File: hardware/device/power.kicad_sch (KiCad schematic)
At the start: 46 parts, among them IC3 SP3401-02UTG, J1 POT_CONN, J2 USB, U20 TPS62A02DRL, U21 TPS560200, U22 BQ24072RGT, U23 BQ21040DBV, U26 BQ25040, U31 FUSB302B01MPX, U32 LTC2942

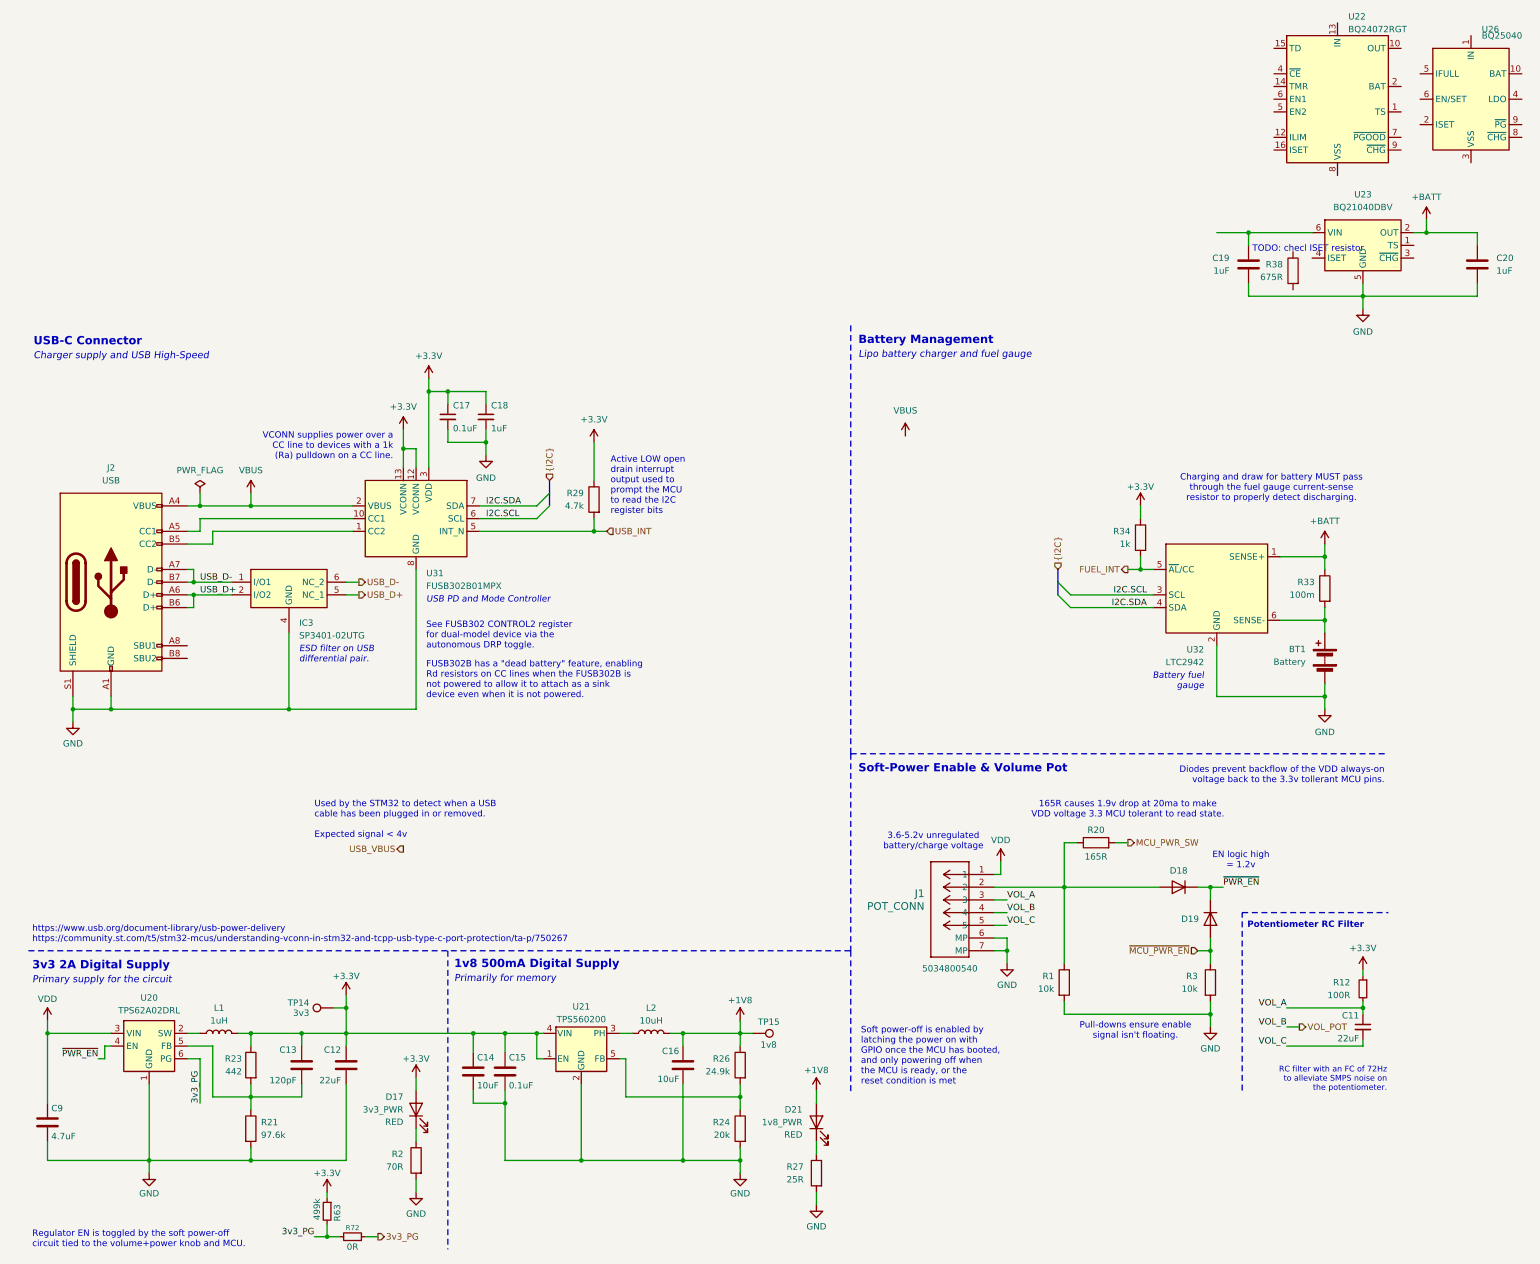
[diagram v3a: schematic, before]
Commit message: feat: various routing, footprint and schematic cleanup
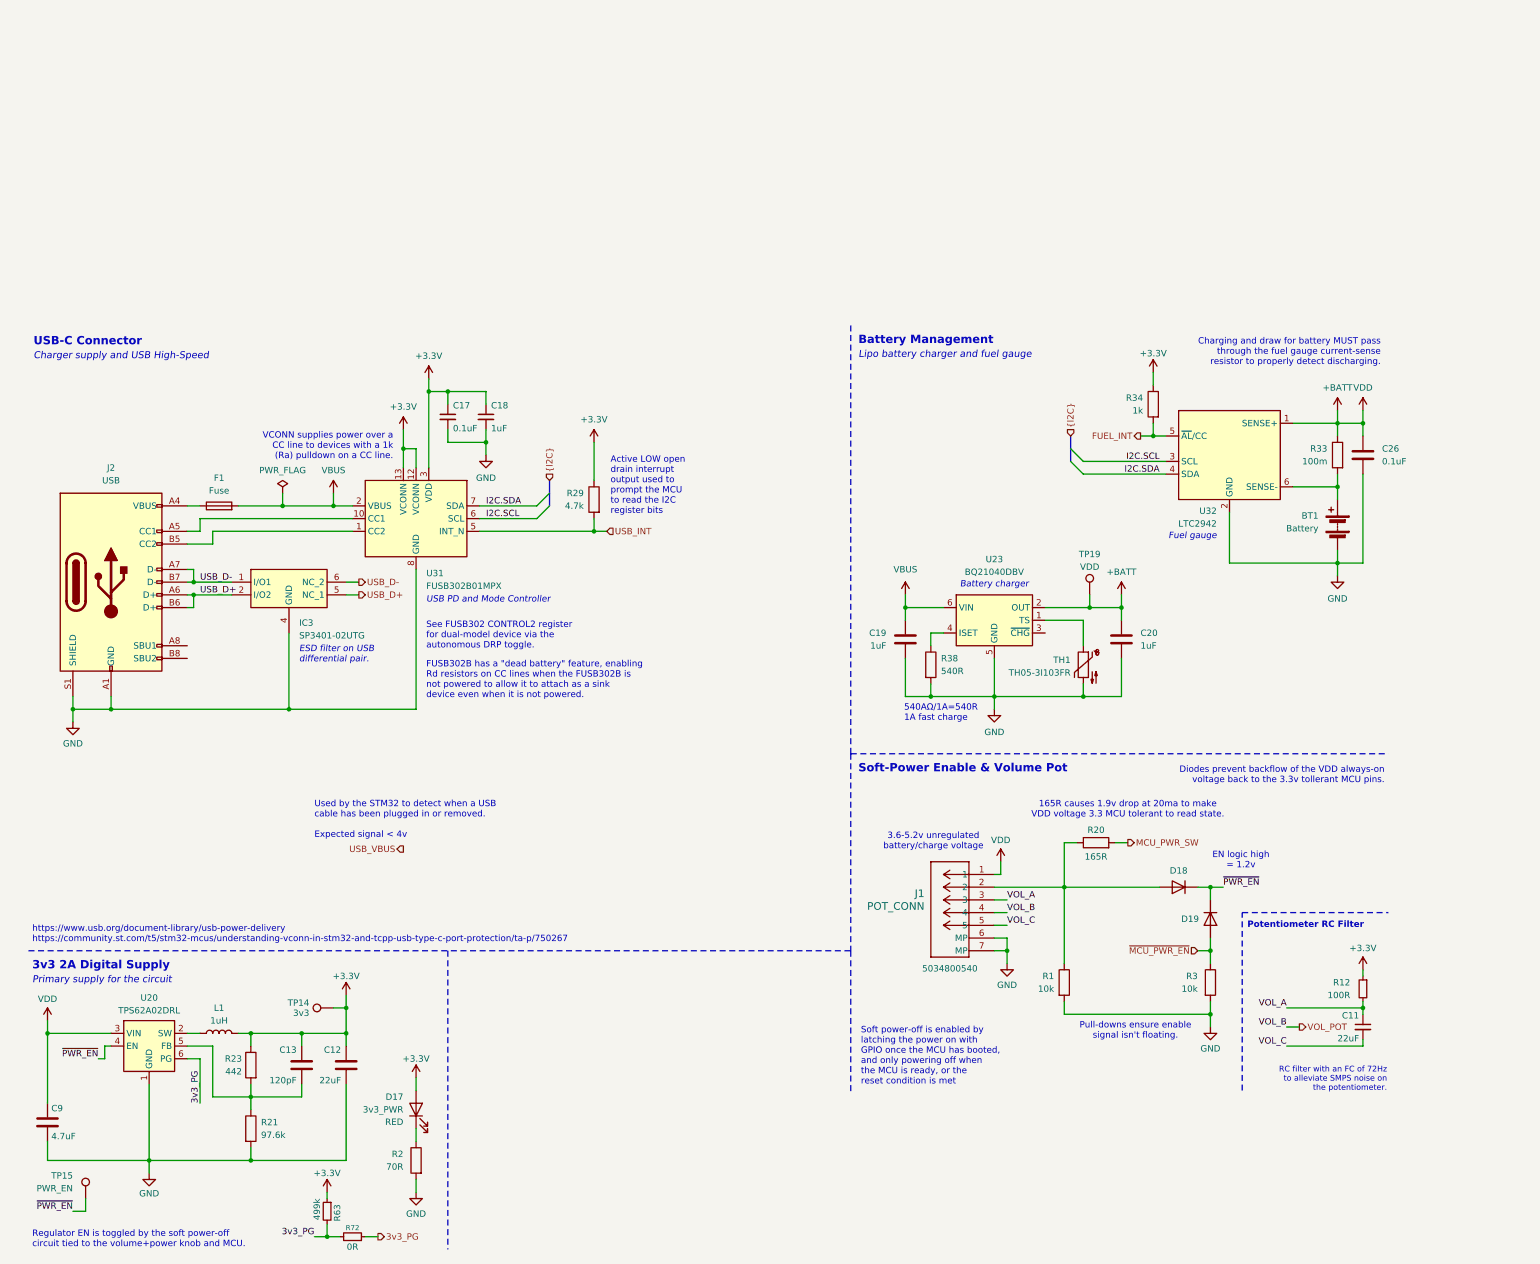
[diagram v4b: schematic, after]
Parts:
- removed C14, C16: 10uF, Capacitor_SMD:C_0402_1005Metric, symbol Device:C
- removed C15: 0.1uF, Capacitor_SMD:C_0402_1005Metric, symbol Device:C
- removed D21: 1v8_PWR, LED_SMD:LED_0805_2012Metric_Pad1.15x1.40mm_HandSolder, symbol Device:LED
- removed L2: 10uH, symbol Device:L
- removed R24: 20k, Capacitor_SMD:C_0402_1005Metric, symbol Device:R
- removed R26: 24.9k, Capacitor_SMD:C_0402_1005Metric, symbol Device:R
- removed R27: 25R, Capacitor_SMD:C_0402_1005Metric, symbol Device:R
- removed U21: TPS560200, Package_TO_SOT_SMD:SOT-23-5, symbol Regulator_Switching:TPS560200
- removed U22: BQ24072RGT, Package_DFN_QFN:VQFN-16-1EP_3x3mm_P0.5mm_EP1.6x1.6mm, symbol Battery_Management:BQ24072RGT
- removed U26: BQ25040, Package_SON:WSON-10-1EP_2x3mm_P0.5mm_EP0.84x2.4mm_ThermalVias, symbol Battery_Management:BQ25040
- added C26: 0.1uF, Capacitor_SMD:C_0603_1608Metric, symbol Device:C
- added F1: Fuse, Fuse:Fuse_0805_2012Metric, symbol Device:Fuse
- added TH1: TH05-3I103FR, Resistor_SMD:R_0402_1005Metric_Pad0.72x0.64mm_HandSolder, symbol Device:Thermistor_NTC
- added TP19: VDD, TestPoint:TestPoint_Pad_D1.0mm, symbol Connector:TestPoint
- C12, C13, C9: footprint Capacitor_SMD:C_0402_1005Metric -> Capacitor_SMD:C_0805_2012Metric
- C19, C20: footprint (none) -> Capacitor_SMD:C_0805_2012Metric
- D18, D19: footprint (none) -> Diode_SMD:D_0603_1608Metric
- L1: footprint (none) -> Inductor_SMD:L_1008_2520Metric; JLC (none) -> C435392
- R21, R23: footprint Capacitor_SMD:C_0402_1005Metric -> Resistor_SMD:R_0603_1608Metric
- R3: footprint (none) -> Resistor_SMD:R_0402_1005Metric
- R38: value 675R -> 540R
- TP15: value 1v8 -> PWR_EN
- U23: JLC (none) -> C78978
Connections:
- net +1V8 is gone; now on net ~{PWR_EN}: TP15.1
- net VDD is gone; now on net +BATT: C9.1, J1.1, U20.3 (VIN)
- net +BATT: now also C26.1, TP19.1
- net GND: now also R38.2, C26.2, TH1.2
- net VBUS: now also C19.1, U23.6 (VIN), F1.2; no longer J2.A4 (VBUS), J2.A9 (VBUS), J2.B4 (VBUS), J2.B9 (VBUS)
- net at R38.1: now also U23.4 (ISET)
- net at U23.1 (TS): now also TH1.1
- new net: F1.1, J2.A4 (VBUS), J2.A9 (VBUS), J2.B4 (VBUS), J2.B9 (VBUS)
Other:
- note added: "540AΩ/1A=540R 1A fast charge"
- note added: "Battery charger"
- note added: "Fuel gauge"
- note removed: "1v8 500mA Digital Supply"
- note removed: "Battery fuel gauge"
- note removed: "Primarily for memory"
- note removed: "TODO: checl ISET resistor"
- moved on the sheet: BT1, C19, C20, R33, R34, R38, U23, U32
